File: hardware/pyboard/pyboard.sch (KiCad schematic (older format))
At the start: 69 parts

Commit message: Remove prefix from lables
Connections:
- net labels added: BLU, BOOT1-MMA-INT, DM, DP, GRN, ID, MMA_AVDD, RED, SCL, SDA, SDIO_CK, SDIO_CMD, SDIO_D0, SDIO_D1, SDIO_D2, SDIO_D3, SDIO_SW, SIDO_CK, SW, X1, X11, X12, X18, X19, X2, X20, X21, X22, X3, X4, X5, X6, X7, X8, Y1, Y10, Y11, Y12, Y2, Y3, Y4, Y5, Y6, Y7, Y8, Y9, YEL
- net labels removed: BOOT0-P1, PA-12DP, PA0-X1, PA1-X2, PA10-ID, PA11-DM, PA12-DP, PA13-RED-P5, PA14-GRN-P4, PA15-YEL-P3, PA2-X3, PA3-X4, PA4-X5, PA5-X6, PA6-X7, PA7-X8, PA8-SDIO_SW, PA9-VBUS, PB0-Y11, PB1-Y12, PB10-Y9, PB11-Y10, PB12-Y5, PB13-Y6, PB14-Y7, PB15-Y8, PB2-BOOT1-MMA-INT, PB3-SW-X17, PB4-BLU-P2, PB5-MMA_AVDD, PB6-SCL, PB6-SCL-X9, PB7-SDA, PB7-SDA-X10, PB8-Y3, PB9-Y4, PC0-X19, PC1-X20, PC10-SDIO_D2, PC11-SDIO_D3, PC12-SDIO_CK, PC12-SIDO_CK, PC13-X18, PC2-X21, PC3-X22, PC4-X11, PC5-X12, PC6-Y1, PC7-Y2, PC8-SDIO_D0, PC9-SDIO_D1, PD2-SDIO_CMD
- wire segments 342 -> 341
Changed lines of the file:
@@
 	6550 6100 5150 6100
-Wire Wire Line
-	5950 6200 5950 6150
 Wire Wire Line
 	6550 6100 6550 6350
@@
 Wire Wire Line
 	6250 6150 6250 6700
-Connection ~ 5950 6150
 Connection ~ 6250 6700
 Wire Wire Line
@@
 USR-SW
 Text Label 9850 9450 0    50   ~ 0
-PB3-SW-X17
+SW
 Wire Wire Line
 	9600 9450 9600 9550
@@
 Wire Wire Line
 	10100 2700 10350 2700
-Text Label 9400 2700 0    50   ~ 0
-PA9-VBUS
 Wire Wire Line
 	9400 2700 9800 2700
@@
 	9800 2900 9400 2900
 Text Label 9400 2900 0    50   ~ 0
-PA12-DP
+DP
 Wire Wire Line
 	9800 3100 9400 3100
 Text Label 9400 3100 0    50   ~ 0
-PA11-DM
+DM
 Text Label 9400 3300 0    50   ~ 0
-PA10-ID
+ID
 Wire Wire Line
 	9800 3300 9400 3300
@@
 Connection ~ 11350 3500
 Text Label 12850 1300 0    50   ~ 0
-PC10-SDIO_D2
+SDIO_D2
 Wire Wire Line
 	13500 1300 12850 1300
@@
 	13500 1400 12850 1400
 Text Label 12850 1400 0    50   ~ 0
-PC11-SDIO_D3
+SDIO_D3
 Wire Wire Line
 	12850 1500 13500 1500
 Text Label 12850 1500 0    50   ~ 0
-PD2-SDIO_CMD
+SDIO_CMD
 Wire Wire Line
 	13500 1700 12850 1700
 Text Label 12850 1700 0    50   ~ 0
-PC12-SIDO_CK
+SIDO_CK
 $Comp
 L power:+3.3V #PWR?
@@
 	12850 1900 13500 1900
 Text Label 12850 1900 0    50   ~ 0
-PC8-SDIO_D0
+SDIO_D0
 Wire Wire Line
 	12850 2000 13500 2000
 Text Label 12850 2000 0    50   ~ 0
-PC9-SDIO_D1
+SDIO_D1
 Text Label 12850 2100 0    50   ~ 0
-PA8-SDIO_SW
+SDIO_SW
 Wire Wire Line
 	13500 2100 12850 2100
@@
 $EndComp
 Text Label 9850 4600 0    50   ~ 0
-PC6-Y1
+Y1
 Text Label 9850 4700 0    50   ~ 0
-PC7-Y2
+Y2
 Text Label 9850 4800 0    50   ~ 0
-PB8-Y3
+Y3
 Text Label 9850 4900 0    50   ~ 0
-PB9-Y4
+Y4
 Text Label 9850 5000 0    50   ~ 0
-PB12-Y5
+Y5
 Text Label 9850 5100 0    50   ~ 0
-PB13-Y6
+Y6
 Text Label 9850 5200 0    50   ~ 0
-PB14-Y7
+Y7
 Text Label 9850 5300 0    50   ~ 0
-PB15-Y8
+Y8
 Text Label 9850 5750 0    50   ~ 0
-PB6-SCL-X9
+SCL
 Wire Wire Line
 	9850 5750 10450 5750
 Text Label 9850 5850 0    50   ~ 0
-PB7-SDA-X10
+SDA
 Text Label 9850 5950 0    50   ~ 0
-PC4-X11
+X11
 Text Label 9850 6050 0    50   ~ 0
-PC5-X12
+X12
 Text Label 9850 6150 0    50   ~ 0
 ~RST
@@
 $EndComp
 Text Label 12450 4600 2    50   ~ 0
-BOOT0-P1
+BOOT0
 Text Label 12450 4700 2    50   ~ 0
-PB4-BLU-P2
+BLU
 Text Label 12450 4800 2    50   ~ 0
-PA15-YEL-P3
+YEL
 Text Label 12450 4900 2    50   ~ 0
-PA14-GRN-P4
+GRN
 Text Label 12450 5000 2    50   ~ 0
-PA13-RED-P5
+RED
 Text Label 12450 5100 2    50   ~ 0
 VRSTIN
@@
 $EndComp
 Text Label 12450 5750 2    50   ~ 0
-PB3-SW-X17
+SW
 Text Label 12450 5850 2    50   ~ 0
-PC13-X18
+X18
 Text Label 12450 5950 2    50   ~ 0
-PC0-X19
+X19
 Text Label 12450 6050 2    50   ~ 0
-PC1-X20
+X20
 Text Label 12450 6150 2    50   ~ 0
-PC2-X21
+X21
 Text Label 12450 6250 2    50   ~ 0
-PC3-X22
+X22
 $Comp
 L Connector_Generic:Conn_02x04_Counter_Clockwise J?
@@
 	2550 4350 1950 4350
 Text Label 1950 4350 0    50   ~ 0
-PD2-SDIO_CMD
+SDIO_CMD
 $Comp
 L Device:Crystal_Small Y?
@@
 	5600 3050 5600 2900
 Text Label 1850 1200 0    50   ~ 0
-PA0-X1
+X1
 Text Label 1850 1300 0    50   ~ 0
-PA1-X2
+X2
 Text Label 1850 1400 0    50   ~ 0
-PA2-X3
+X3
 Text Label 1850 1500 0    50   ~ 0
-PA3-X4
+X4
 Text Label 1850 1600 0    50   ~ 0
-PA4-X5
+X5
 Text Label 1850 1700 0    50   ~ 0
-PA5-X6
+X6
 Text Label 1850 1800 0    50   ~ 0
-PA6-X7
+X7
 Text Label 1850 1900 0    50   ~ 0
-PA7-X8
+X8
 Text Label 1850 2000 0    50   ~ 0
-PA8-SDIO_SW
+SDIO_SW
 Text Label 1850 2100 0    50   ~ 0
-PA9-VBUS
+VBUS
 Text Label 1850 2200 0    50   ~ 0
-PA10-ID
+ID
 Text Label 1850 2300 0    50   ~ 0
-PA11-DM
+DM
 Text Label 1850 2400 0    50   ~ 0
-PA-12DP
+DP
 Text Label 1850 2500 0    50   ~ 0
-PA13-RED-P5
+RED
 Text Label 1850 2600 0    50   ~ 0
-PA14-GRN-P4
+GRN
 Text Label 1850 2700 0    50   ~ 0
-PA15-YEL-P3
+YEL
 Wire Wire Line
 	2550 1200 1850 1200
@@
 $EndComp
 Text Label 4950 4150 2    50   ~ 0
-PC13-X18
+X18
 Text Label 4950 4250 2    50   ~ 0
 N1
@@
 N2
 Text Label 4950 1200 2    50   ~ 0
-PB0-Y11
+Y11
 Text Label 4950 1300 2    50   ~ 0
-PB1-Y12
+Y12
 Text Label 4950 1500 2    50   ~ 0
-PB3-SW-X17
+SW
 Text Label 4950 1600 2    50   ~ 0
-PB4-BLU-P2
+BLU
 Text Label 4950 1700 2    50   ~ 0
-PB5-MMA_AVDD
+MMA_AVDD
 Text Label 4950 1800 2    50   ~ 0
-PB6-SCL-X9
+SCL
 Text Label 4950 1900 2    50   ~ 0
-PB7-SDA-X10
+SDA
 Text Label 4950 2000 2    50   ~ 0
-PB8-Y3
+Y3
 Text Label 4950 2100 2    50   ~ 0
-PB9-Y4
+Y4
 Text Label 4950 2200 2    50   ~ 0
-PB10-Y9
+Y9
 Text Label 4950 2300 2    50   ~ 0
-PB11-Y10
+Y10
 Text Label 4950 2400 2    50   ~ 0
-PB12-Y5
+Y5
 Text Label 4950 2500 2    50   ~ 0
-PB13-Y6
+Y6
 Text Label 4950 2600 2    50   ~ 0
-PB14-Y7
+Y7
 Text Label 4950 2700 2    50   ~ 0
-PB15-Y8
+Y8
 Text Label 4950 2850 2    50   ~ 0
-PC0-X19
+X19
 Text Label 4950 2950 2    50   ~ 0
-PC1-X20
+X20
 Text Label 4950 3050 2    50   ~ 0
-PC2-X21
+X21
 Text Label 4950 3150 2    50   ~ 0
-PC3-X22
+X22
 Text Label 4950 3250 2    50   ~ 0
-PC4-X11
+X11
 Text Label 4950 3350 2    50   ~ 0
-PC5-X12
+X12
 Text Label 4950 3450 2    50   ~ 0
-PC6-Y1
+Y1
 Text Label 4950 3550 2    50   ~ 0
-PC7-Y2
+Y2
 Text Label 4950 3650 2    50   ~ 0
-PC8-SDIO_D0
+SDIO_D0
 Text Label 4950 3750 2    50   ~ 0
-PC9-SDIO_D1
+SDIO_D1
 Text Label 4950 3850 2    50   ~ 0
-PC10-SDIO_D2
+SDIO_D2
 Text Label 4950 3950 2    50   ~ 0
-PC11-SDIO_D3
+SDIO_D3
 Text Label 4950 4050 2    50   ~ 0
-PC12-SDIO_CK
+SDIO_CK
 Text Label 4950 1400 2    50   ~ 0
-PB2-BOOT1-MMA-INT
+BOOT1-MMA-INT
 Wire Wire Line
 	4950 1200 3850 1200
@@
 ~RST
 Text Label 14050 5000 2    50   ~ 0
-PB1-Y12
+Y12
 Text Label 14050 5100 2    50   ~ 0
-PB0-Y11
+Y11
 Text Label 14050 5200 2    50   ~ 0
-PB11-Y10
+Y10
 Text Label 14050 5300 2    50   ~ 0
-PB10-Y9
+Y9
 $Comp
 L Connector_Generic:Conn_01x08 J?
@@
 	14050 5850 13550 5850
 Text Label 13750 6450 0    50   ~ 0
-PA0-X1
+X1
 Text Label 13750 6350 0    50   ~ 0
-PA1-X2
+X2
 Text Label 13750 6250 0    50   ~ 0
-PA2-X3
+X3
 Text Label 13750 6150 0    50   ~ 0
-PA3-X4
+X4
 Text Label 13750 6050 0    50   ~ 0
-PA4-X5
+X5
 Text Label 13750 5950 0    50   ~ 0
-PA5-X6
+X6
 Text Label 13750 5850 0    50   ~ 0
-PA6-X7
+X7
 Wire Wire Line
 	13550 5750 14050 5750
 Text Label 13750 5750 0    50   ~ 0
-PA7-X8
+X8
 $Comp
 L Connector_Generic:Conn_01x08 J?
@@
 	13900 8600 13250 8600
 Text Label 13250 8600 0    50   ~ 0
-PB4-BLU-P2
+BLU
 Wire Wire Line
 	13900 8250 13250 8250
 Text Label 13250 8250 0    50   ~ 0
-PA15-YEL-P3
+YEL
 Wire Wire Line
 	13900 7900 13250 7900
 Text Label 13250 7900 0    50   ~ 0
-PA14-GRN-P4
+GRN
 Wire Wire Line
 	13900 7550 13250 7550
 Text Label 13250 7550 0    50   ~ 0
-PA13-RED-P5
+RED
 Text Label 14350 8600 0    50   ~ 0
 B
@@
 	9050 8400 10200 8400
 Text Label 9050 8400 0    50   ~ 0
-PB2-BOOT1-MMA-INT
+BOOT1-MMA-INT
 Text Label 12150 8300 0    50   ~ 0
-PB7-SDA
+SDA
 Wire Wire Line
 	11900 7650 11900 8100
@@
 	11900 7550 11900 7650
 Text Label 12150 8400 0    50   ~ 0
-PB6-SCL
+SCL
 Connection ~ 11700 8200
 Wire Wire Line
@@
 $EndComp
 Text Label 9700 7600 0    50   ~ 0
-PB5-MMA_AVDD
+MMA_AVDD
 Wire Wire Line
 	11700 8200 11500 8200
@@
 Text Notes 8900 9300 0    100  ~ 0
 Programmable button
+Text Label 9400 2700 0    50   ~ 0
+VBUS
 $EndSCHEMATC

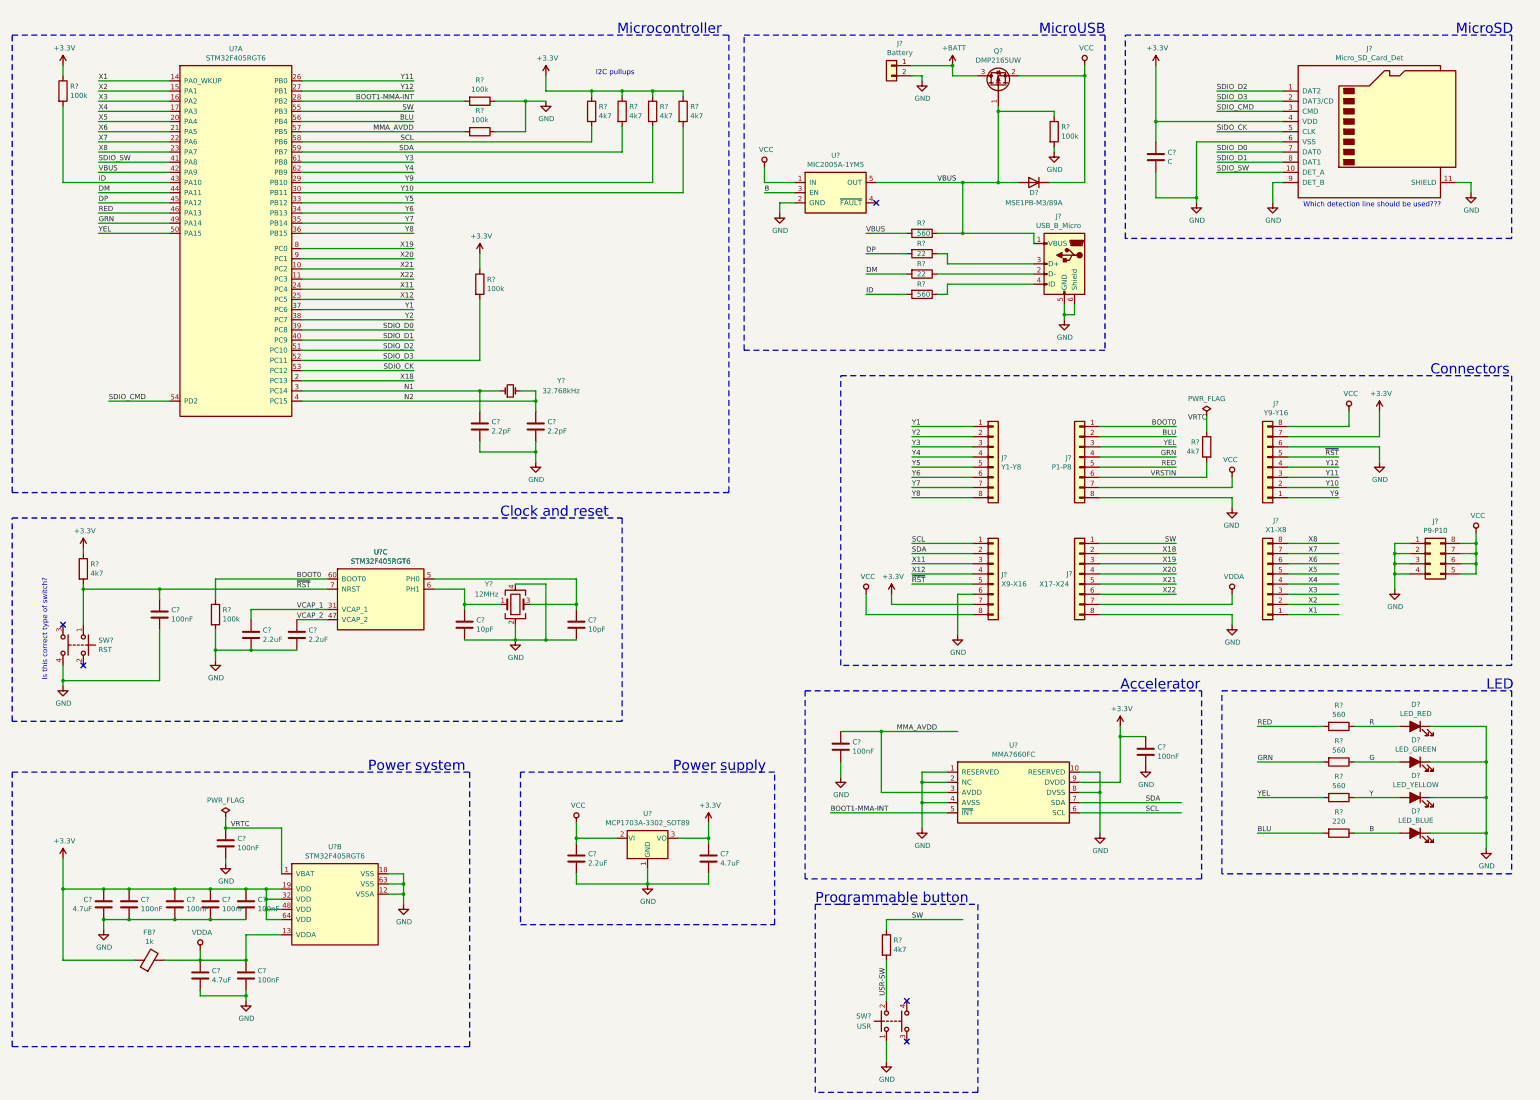
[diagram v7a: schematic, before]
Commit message: Annotate schmatics
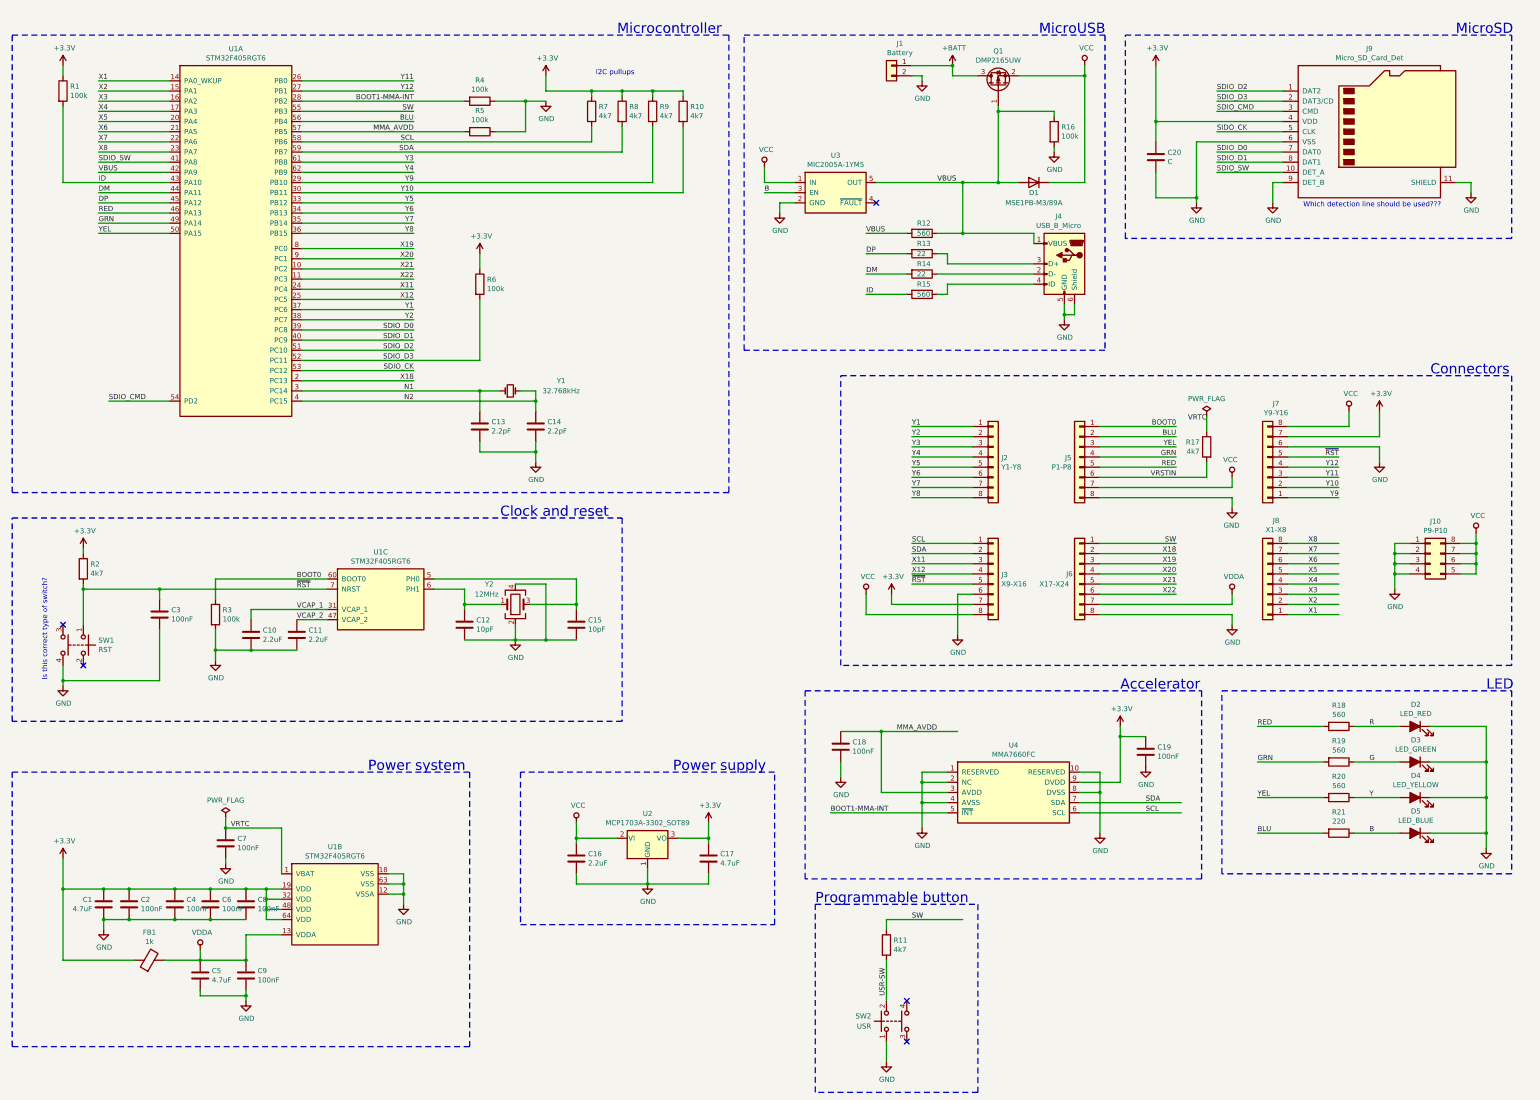
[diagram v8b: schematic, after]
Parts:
- removed U?: STM32F405RGT6, symbol components:STM32F405RGT6
- removed U?: STM32F405RGT6, symbol pyboard-rescue:STM32F405RGT6-components
- added unit 3 of U1
- gave numbers to parts that had none: 66
